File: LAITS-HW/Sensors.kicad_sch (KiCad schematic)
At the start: 25 parts, among them U301 DS18B20, U302 AS7341, U303 BH1750FVI-TR, U304 TCS34725FN, U305 TSL2561, U306 PCA9306GM,125

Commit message: generate IBOM
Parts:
- R304, R305: Place (none) -> DNP
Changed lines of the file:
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@@
+      (effects (font (size 1.27 1.27)) hide)
+    )
+    (property "Place" "DNP" (id 4) (at 81.28 127.635 0)
       (effects (font (size 1.27 1.27)) hide)
     )
@@
       (effects (font (size 1.27 1.27)) hide)
     )
+    (property "Place" "DNP" (id 4) (at 78.105 127.635 0)
+      (effects (font (size 1.27 1.27)) hide)
+    )

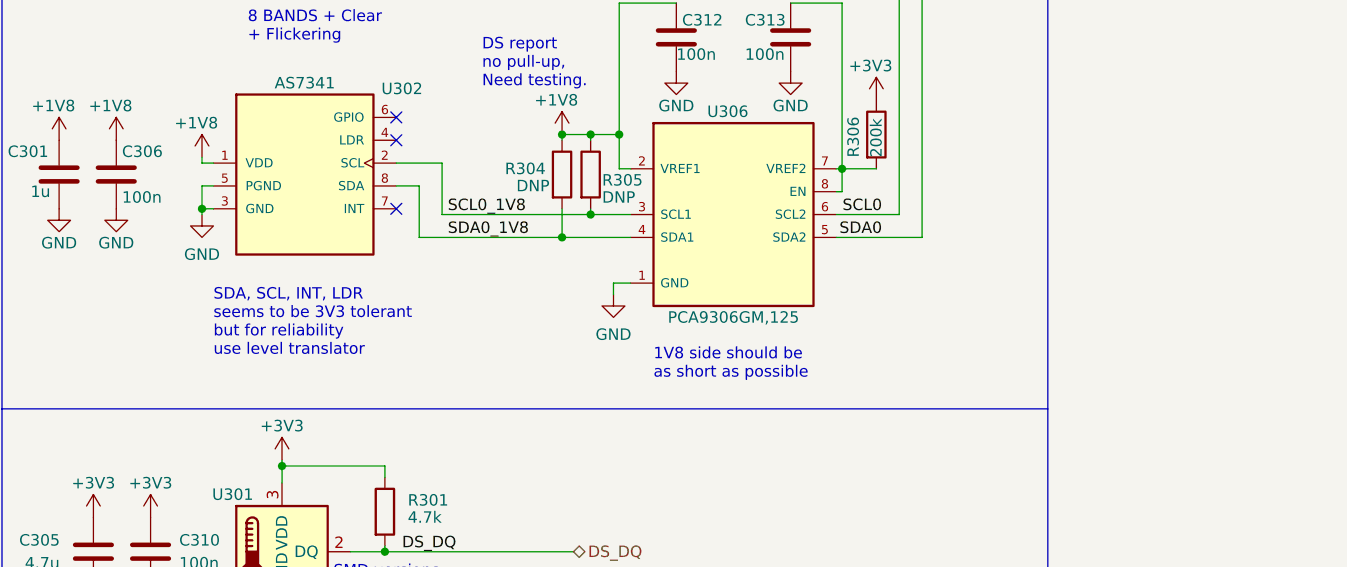
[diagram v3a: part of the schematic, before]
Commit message: Now LAITS notify charge state also when turned off
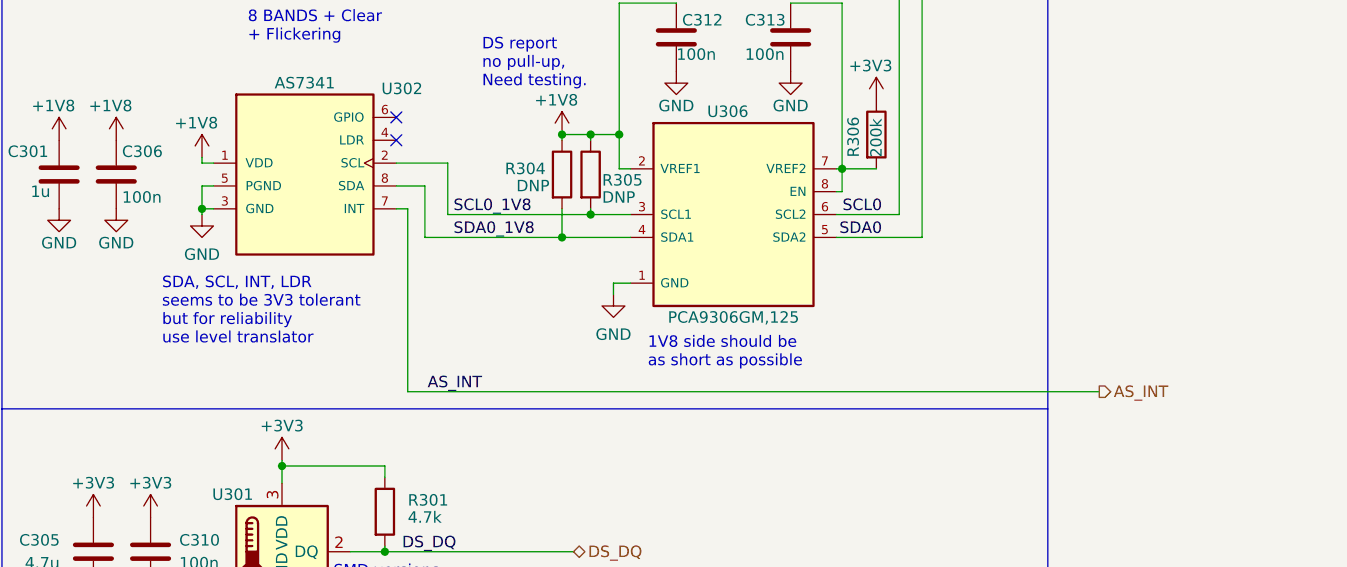
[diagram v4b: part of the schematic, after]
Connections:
- net AS_INT: now reaches U302.7 (INT)
- no-connect marks 5 -> 4
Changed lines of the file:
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@@
   (title_block
     (title "Sensors")
-    (date "2022-08-11")
-    (rev "1.0.2")
+    (date "2022-08-12")
+    (rev "1.0.3")
     (company "Simone Tollardo")
   )
@@
   (no_connect (at 62.865 40.005))
   (no_connect (at 62.865 97.155))
-  (no_connect (at 59.69 131.445))
   (wire (pts (xy 115.57 74.93) (xy 115.57 92.075))
     (stroke (width 0) (type default) (color 0 0 0 0))
@@
     (stroke (width 0) (type default) (color 0 0 0 0))
   )
+  (wire (pts (xy 60.96 151.765) (xy 137.795 151.765))
+    (stroke (width 0) (type default) (color 0 0 0 0))
+  )
   (wire (pts (xy 85.725 127) (xy 84.455 127))
     (stroke (width 0) (type default) (color 0 0 0 0))
@@
     (stroke (width 0) (type default) (color 0 0 0 0))
   )
-  (wire (pts (xy 62.23 128.905) (xy 62.23 134.62))
+  (wire (pts (xy 62.865 128.905) (xy 62.865 134.62))
     (stroke (width 0) (type default) (color 0 0 0 0))
   )
@@
     (stroke (width 0) (type default) (color 0 0 0 0))
   )
-  (wire (pts (xy 59.69 126.365) (xy 64.77 126.365))
-    (stroke (width 0) (type default) (color 0 0 0 0))
-  )
-  (wire (pts (xy 64.77 132.08) (xy 81.28 132.08))
+  (wire (pts (xy 59.69 126.365) (xy 65.405 126.365))
+    (stroke (width 0) (type default) (color 0 0 0 0))
+  )
+  (wire (pts (xy 65.405 132.08) (xy 81.28 132.08))
     (stroke (width 0) (type default) (color 0 0 0 0))
   )
@@
     (stroke (width 0) (type default) (color 0 0 0 0))
   )
-  (wire (pts (xy 59.69 128.905) (xy 62.23 128.905))
+  (wire (pts (xy 59.69 128.905) (xy 62.865 128.905))
     (stroke (width 0) (type default) (color 0 0 0 0))
   )
@@
     (stroke (width 0) (type default) (color 0 0 0 0))
   )
-  (wire (pts (xy 64.77 132.08) (xy 64.77 126.365))
+  (wire (pts (xy 65.405 132.08) (xy 65.405 126.365))
     (stroke (width 0) (type default) (color 0 0 0 0))
   )
@@
     (stroke (width 0) (type default) (color 0 0 0 0))
   )
+  (wire (pts (xy 60.96 131.445) (xy 60.96 151.765))
+    (stroke (width 0) (type default) (color 0 0 0 0))
+  )
   (wire (pts (xy 103.505 108.585) (xy 109.22 108.585))
     (stroke (width 0) (type default) (color 0 0 0 0))
@@
     (stroke (width 0) (type default) (color 0 0 0 0))
   )
+  (wire (pts (xy 60.96 131.445) (xy 59.69 131.445))
+    (stroke (width 0) (type default) (color 0 0 0 0))
+  )
   (wire (pts (xy 108.585 127) (xy 109.22 127))
     (stroke (width 0) (type default) (color 0 0 0 0))
   )
-  (wire (pts (xy 62.23 134.62) (xy 78.105 134.62))
+  (wire (pts (xy 62.865 134.62) (xy 78.105 134.62))
     (stroke (width 0) (type default) (color 0 0 0 0))
   )
@@
     (effects (font (size 1.27 1.27)) (justify left bottom))
   )
-  (text "1V8 side should be\nas short as possible" (at 88.265 150.495 0)
+  (text "1V8 side should be\nas short as possible" (at 87.63 149.225 0)
     (effects (font (size 1.27 1.27)) (justify left bottom))
   )
@@
   )
   (text "SDA, SCL, INT, LDR\nseems to be 3V3 tolerant\nbut for reliability\nuse level translator"
-    (at 39.37 147.955 0)
+    (at 33.655 146.685 0)
     (effects (font (size 1.27 1.27)) (justify left bottom))
   )
@@
     (effects (font (size 1.27 1.27)) (justify left bottom))
   )
-  (label "SDA0_1V8" (at 65.405 134.62 0)
+  (label "SDA0_1V8" (at 66.04 134.62 0)
     (effects (font (size 1.27 1.27)) (justify left bottom))
   )
@@
   (label "SDA0" (at 63.5 37.465 0)
     (effects (font (size 1.27 1.27)) (justify left bottom))
+  )
+  (label "AS_INT" (at 69.215 151.765 180)
+    (effects (font (size 1.27 1.27)) (justify right bottom))
   )
   (label "SDA0" (at 63.5 94.615 0)
@@
     (effects (font (size 1.27 1.27)) (justify right bottom))
   )
-  (label "SCL0_1V8" (at 65.405 132.08 0)
+  (label "SCL0_1V8" (at 66.04 132.08 0)
     (effects (font (size 1.27 1.27)) (justify left bottom))
   )
@@
     (effects (font (size 1.27 1.27)) (justify left bottom))
   )
+  (hierarchical_label "AS_INT" (shape output) (at 137.795 151.765 0)
+    (effects (font (size 1.27 1.27)) (justify left))
+  )
   (hierarchical_label "SDA0" (shape bidirectional) (at 137.795 77.47 0)
